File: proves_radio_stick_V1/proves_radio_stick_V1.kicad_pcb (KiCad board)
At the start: 4 copper layers, 88 x 94.5 mm, 54 parts, among them IC2 AZ1117CH-3.3TRG1, J12 USB_C_Receptacle_USB2.0_16P, J22 SWD Port, SW1 KMR2, SW2 KMR2, SW3 SW_Push_SPDT, U11 W25Q128JVS, U18 RP2350_60QFN, Y1 ABM8-272-T3

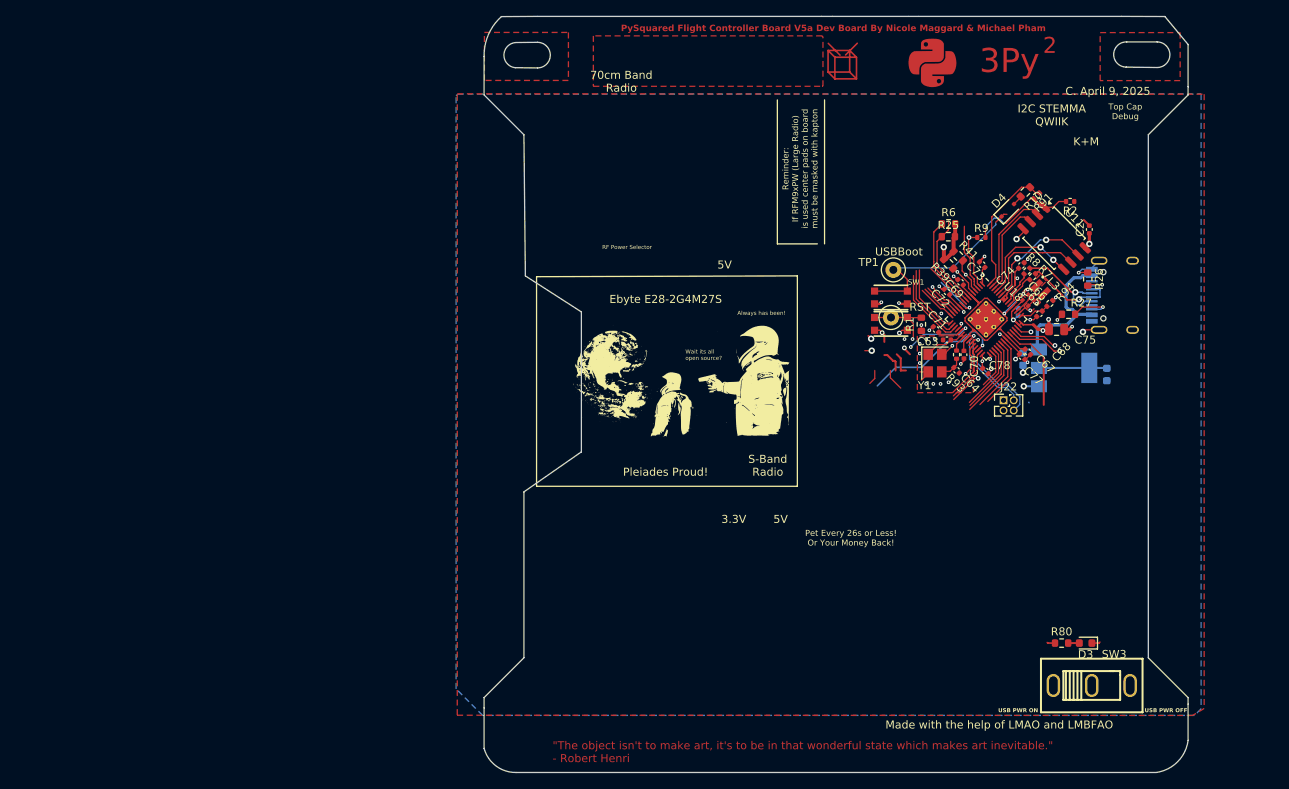
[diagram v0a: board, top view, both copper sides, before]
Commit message: Removed V0a Project
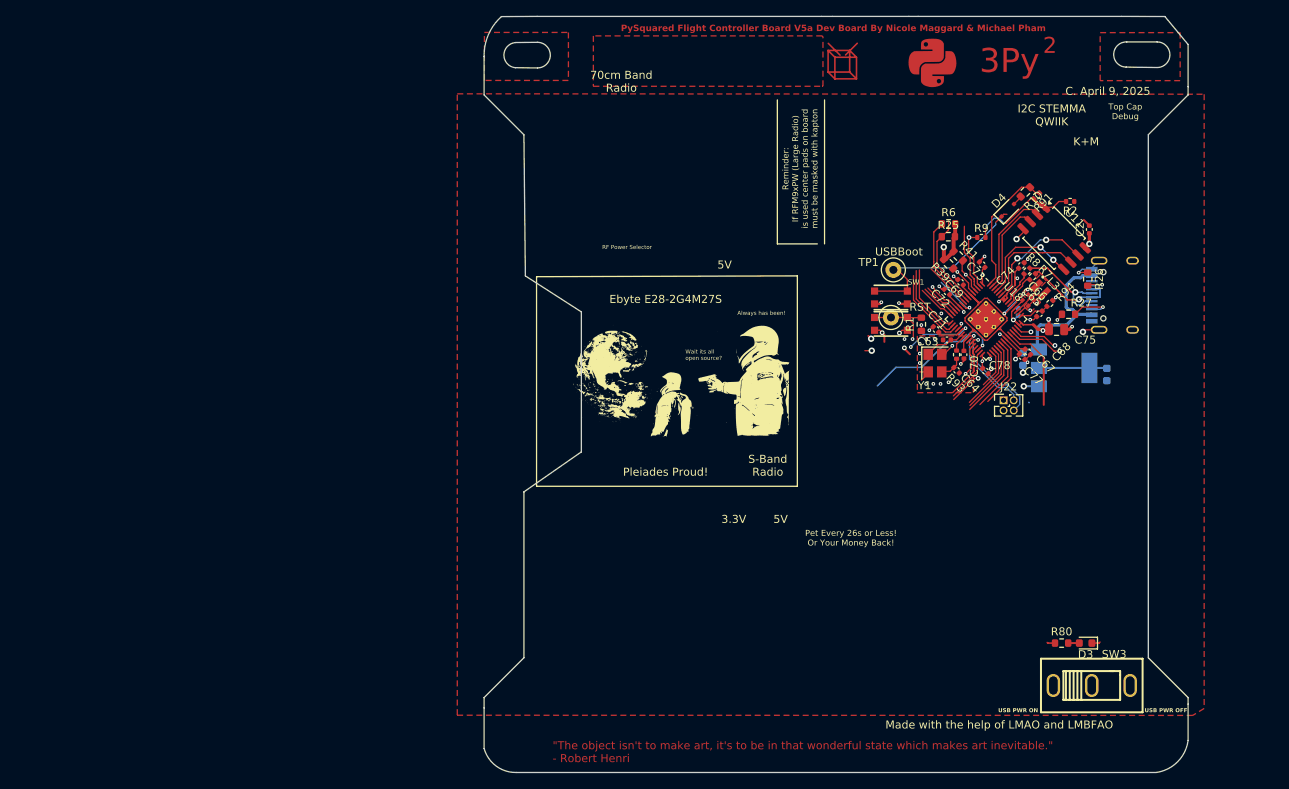
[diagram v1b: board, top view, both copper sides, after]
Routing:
- net (no net): track 9.08 -> 1.48 mm
- net ~{GPIO_EXPANDER_RESET}: track 7.63 -> 4.90 mm
- removed copper zone on B.Cu, net GND
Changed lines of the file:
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@@
 	)
 	(segment
-		(start 195.425 90.3)
-		(end 194.925 89.8)
-		(width 0.25)
-		(layer "F.Cu")
-		(net 0)
-	)
-	(segment
-		(start 192.175 91.825)
-		(end 192.175 92.8294)
-		(width 0.1524)
-		(layer "F.Cu")
-		(net 0)
-	)
-	(segment
-		(start 194.775 91.825)
-		(end 194.775 90.723001)
-		(width 0.25)
-		(layer "F.Cu")
-		(net 0)
-	)
-	(segment
-		(start 195.425 91.825)
-		(end 195.425 90.3)
-		(width 0.25)
-		(layer "F.Cu")
-		(net 0)
-	)
-	(segment
-		(start 192.175 92.8294)
-		(end 191.562475 93.441925)
-		(width 0.1524)
-		(layer "F.Cu")
-		(net 0)
-	)
-	(segment
-		(start 193.75 89.9)
-		(end 193.375 89.9)
-		(width 0.25)
-		(layer "F.Cu")
-		(net 0)
-	)
-	(segment
-		(start 194.676 90.624001)
-		(end 194.474001 90.624001)
-		(width 0.25)
-		(layer "F.Cu")
-		(net 0)
-	)
-	(segment
-		(start 194.474001 90.624001)
-		(end 193.75 89.9)
-		(width 0.25)
-		(layer "F.Cu")
-		(net 0)
-	)
-	(segment
 		(start 191.72272 87.850001)
 		(end 191.374 87.501281)
@@
 		(net 0)
 	)
-	(segment
-		(start 195.425 91.825)
-		(end 196.075 91.825)
-		(width 0.25)
-		(layer "F.Cu")
-		(net 0)
-	)
-	(segment
-		(start 194.775 90.723001)
-		(end 194.676 90.624001)
-		(width 0.25)
-		(layer "F.Cu")
-		(net 0)
-	)
 	(via
 		(at 191.72272 87.850001)
@@
 	)
 	(segment
-		(start 194.125 92.725)
-		(end 195.4238 94.0238)
-		(width 0.1524)
-		(layer "F.Cu")
-		(net 56)
-	)
-	(segment
-		(start 194.125 91.825001)
-		(end 194.125 92.725)
-		(width 0.1524)
-		(layer "F.Cu")
-		(net 56)
-	)
-	(segment
 		(start 207.3 92.048862)
 		(end 207.3 90.032753)
@@
 			)
 		)
-	)
-	(zone
-		(net 1)
-		(net_name "GND")
-		(layer "B.Cu")
-		(hatch edge 0.5)
-		(priority 4)
-		(connect_pads
-			(clearance 0.5)
-		)
-		(min_thickness 0.25)
-		(filled_areas_thickness no)
-		(fill yes
-			(thermal_gap 0.5)
-			(thermal_bridge_width 0.5)
-		)
-		(polygon
-			(pts
-				(xy 140.07 57.27) (xy 232.97 57.27) (xy 232.97 134.11) (xy 232.14 134.94) (xy 143.16 134.94) (xy 139.84 131.62)
-				(xy 139.84 57.5)
-			)
-		)

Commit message: Initial TPS62 Layout
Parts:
- added C14: 22uF, Capacitor_SMD:C_0603_1608Metric, F.Cu at (212.3, 107.8)
- added C15: 10uF, Capacitor_SMD:C_0603_1608Metric, F.Cu at (210.0, 107.0)
- added L1: XFL4015-471MEC, easyeda2kicad:IND-SMD_L4.0-W4.0_XFL4020-102MEB, F.Cu at (211.1, 104.0)
- added R3: 162k, Resistor_SMD:R_0603_1608Metric, F.Cu at (212.3, 110.8)
- added R4: 510k, Resistor_SMD:R_0603_1608Metric, F.Cu at (210.0, 111.6)
- added U1: E22-400M30S, easyeda2kicad:WIRELM-SMD_E22-400M30S, F.Cu at (98.2, 74.6)
- added U2: TPS62085RLTT, easyeda2kicad:VSON-7_L2.0-W2.0-P0.5-TL, F.Cu at (210.0, 109.3)
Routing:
- net SPI1_CS1: track 14.4 -> 1.05 mm
- net RF2_IO0: track 10.0 -> 4.00 mm
- net RF2_TX_EN: track 9.08 -> 3.57 mm
- net RF2_RX_EN: track 8.29 -> 3.13 mm
- net WDT_WDI: track 9.46 -> 4.54 mm
- net Net-(U2-SW): track 0.00 -> 4.50 mm
- net SPI1_SCK: track 6.80 -> 2.56 mm
- net SPI1_MOSI: track 7.78 -> 3.62 mm
- net WDT_ENABLE: track 9.17 -> 5.07 mm
- net +3V3: track 81.2 -> 85.2 mm, vias 18 -> 19
- net SPI1_MISO: track 6.96 -> 3.14 mm
- net Net-(U2-FB): track 0.00 -> 3.35 mm
- net GND: track 50.2 -> 47.4 mm, vias 34 -> 40
- net ~{GPIO_EXPANDER_RESET}: track 4.90 -> 2.70 mm
- net (no net): track 1.48 -> 0.07 mm, vias 1 -> 0

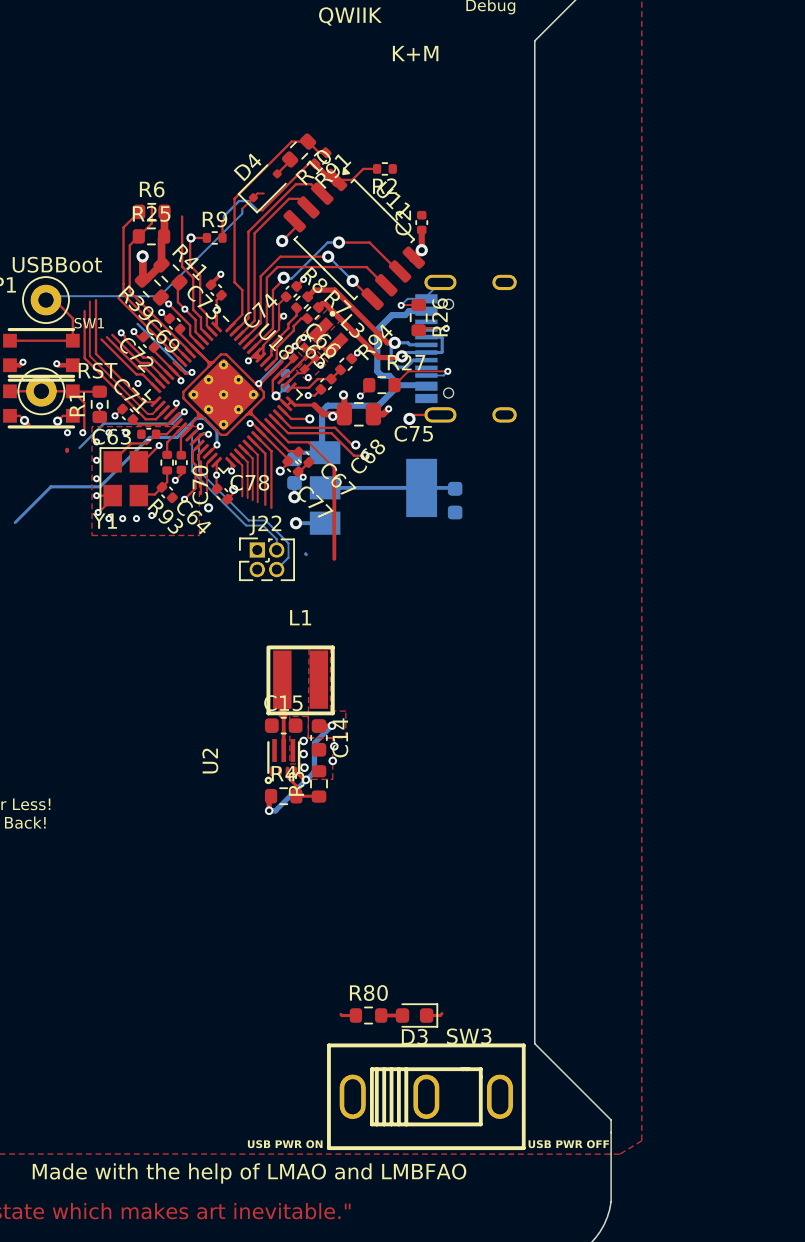
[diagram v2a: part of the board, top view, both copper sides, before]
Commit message: Removed 3v3 Linear Regulator
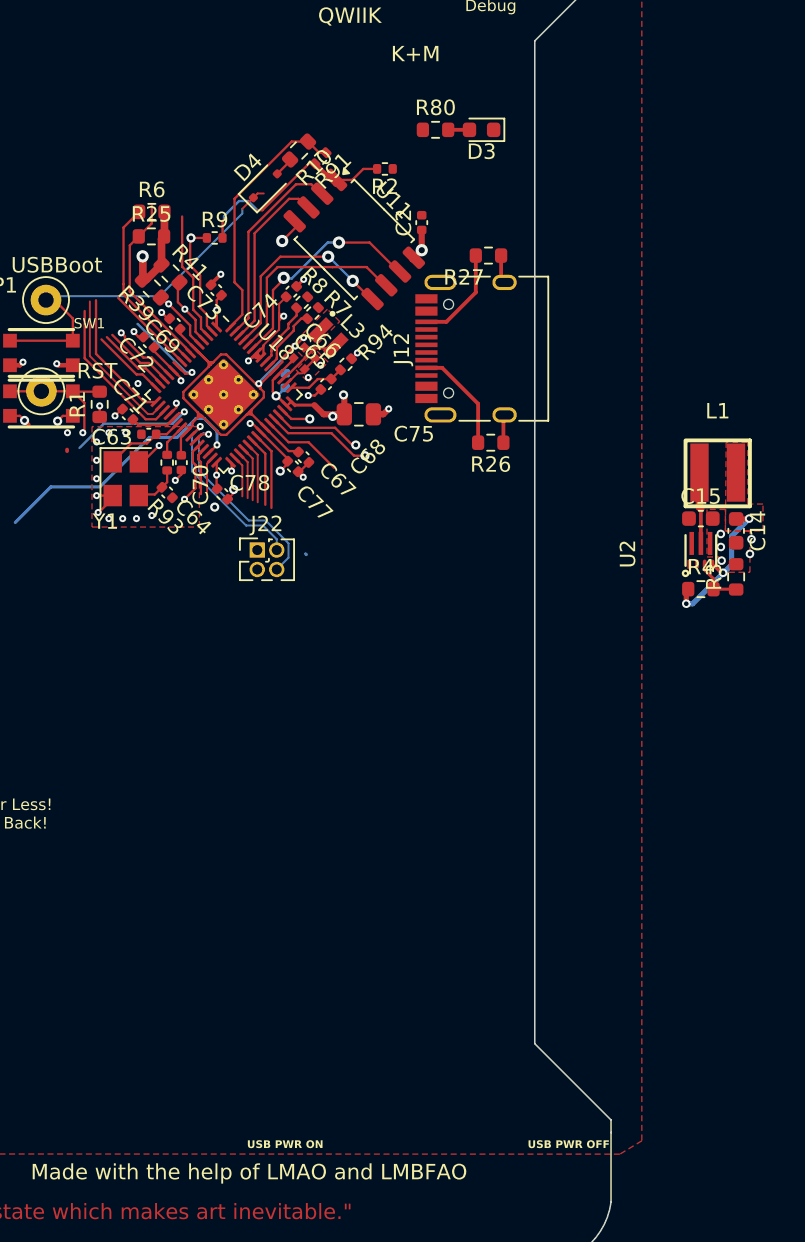
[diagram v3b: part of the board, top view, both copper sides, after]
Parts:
- removed C12: 10uF, Capacitor_SMD:C_0603_1608Metric
- removed C13: 22uF, Capacitor_SMD:C_0603_1608Metric
- removed IC2: AZ1117CH-3.3TRG1, Package_TO_SOT_SMD:SOT-223
- removed SW3: SW_Push_SPDT, easyeda2kicad:SW-TH_SHOU-HAN_SS12D10G4
- J12: moved to F.Cu
- R80: value 100k -> 10k
- moved D3 57.9 mm to (222.9, 68.2)
- moved R80 57.9 mm to (219.9, 68.2)
- moved L1 30.4 mm to (238.3, 90.5)
- moved C14 30.4 mm to (239.5, 94.3)
- moved C15 30.4 mm to (237.2, 93.5)
- moved R3 30.4 mm to (239.5, 97.3)
- moved R4 30.4 mm to (237.2, 98.1)
- moved U2 30.4 mm to (237.2, 95.8)
- moved R27 10.9 mm to (223.3, 76.3), turned to 180 degrees
- moved R26 9.41 mm to (223.5, 88.5), turned to 180 degrees
- turned J12 to 90 degrees
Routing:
- net VBUS: track 21.1 -> 0.00 mm
- net USB_D+: track 13.9 -> 0.00 mm, vias 1 -> 0
- net USB_D-: track 11.7 -> 0.00 mm, vias 1 -> 0
- net /3v3 Spec: track 8.39 -> 0.00 mm
- net GND: track 47.4 -> 39.7 mm, vias 40 -> 35
- net ~{MUX_RESET}: track 11.4 -> 5.43 mm
- net Net-(J12-CC1): track 3.18 -> 6.88 mm, vias 1 -> 0
- net Net-(J12-CC2): track 5.35 -> 6.42 mm, vias 1 -> 0
- net +3V3: track 85.2 -> 84.1 mm

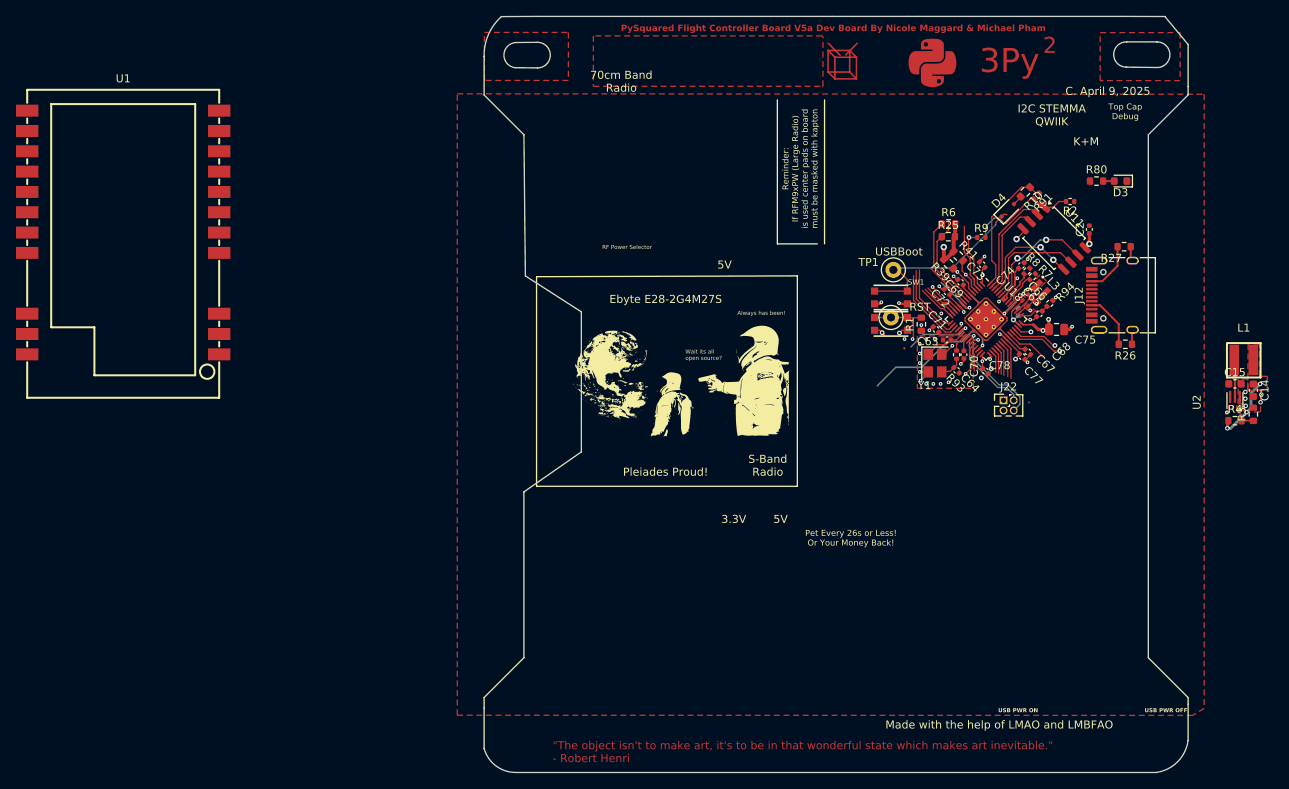
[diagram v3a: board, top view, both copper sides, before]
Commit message: RP2350 and Support Circuits Layout
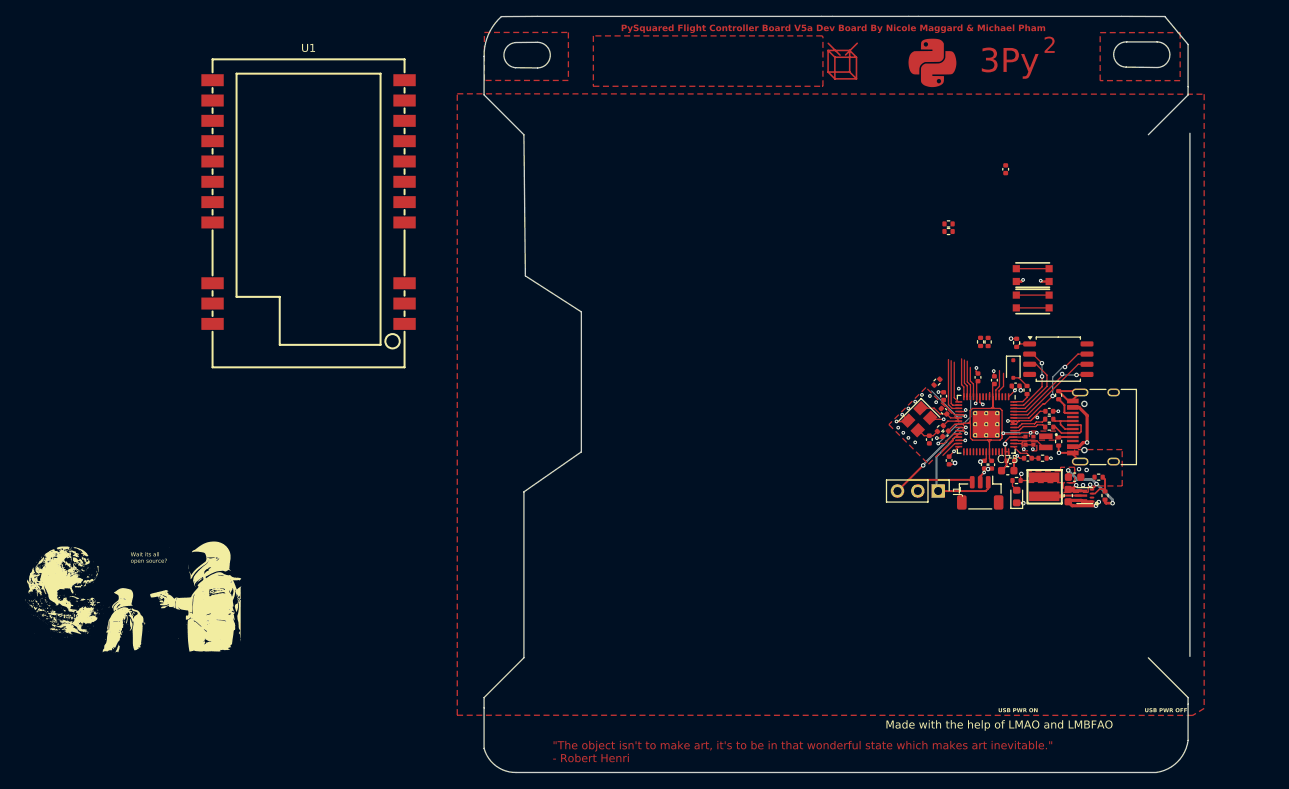
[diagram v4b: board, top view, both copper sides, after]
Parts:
- removed the G*** at (186.3, 67.3)
- removed R9: DNF, Resistor_SMD:R_0402_1005Metric
- removed R91: 0, Resistor_SMD:R_0402_1005Metric
- removed TP1: USBBOOT, TestPoint:TestPoint_Loop_D1.80mm_Drill1.0mm_Beaded
- removed TP2: RESET, TestPoint:TestPoint_Loop_D1.80mm_Drill1.0mm_Beaded
- added J1: SWD Port, Connector_PinHeader_2.54mm:PinHeader_1x03_P2.54mm_Vertical, F.Cu at (200.1, 106.9)
- C75: footprint Capacitor_SMD:C_0805_2012Metric -> Capacitor_SMD:C_0603_1608Metric
- C76: moved to F.Cu
- J22: footprint Connector_PinHeader_1.27mm:PinHeader_2x02_P1.27mm_Vertical -> Connector_JST:JST_SH_BM03B-SRSS-TB_1x03-1MP_P1.00mm_Vertical
- R1, R10, R25, R26, R27, R3, R39, R4, R41, R6, R80: footprint Resistor_SMD:R_0603_1608Metric -> Resistor_SMD:R_0402_1005Metric
- moved G*** 73.6 mm to (98.6, 119.7)
- moved D3 41.5 mm to (209.9, 107.6), turned to 90 degrees
- moved R80 38.7 mm to (209.9, 105.6), turned to 180 degrees
- moved L1 29.6 mm to (213.4, 106.4), turned to 90 degrees
- moved C15 25.1 mm to (216.4, 107.5), turned to 90 degrees
- moved C14 24.8 mm to (217.2, 105.2), turned to 0 degrees
- moved R10 24.8 mm to (211.2, 94.3), turned to 90 degrees
- moved U1 23.5 mm to (121.4, 70.8)
- moved U2 21.9 mm to (218.7, 107.5), turned to 180 degrees
- moved R3 20.9 mm to (220.2, 105.2), turned to 180 degrees
- moved R27 20.3 mm to (215.2, 94.9), turned to -90 degrees
- moved D4 19.9 mm to (209.5, 91.6), turned to -90 degrees
- moved R94 19.4 mm to (213.2, 102.8), turned to 180 degrees
- moved L3 19.1 mm to (213.6, 100.7), turned to -90 degrees
- moved R7 18.9 mm to (214.0, 98.9), turned to 0 degrees
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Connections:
- J22 pad 1: FC_RESET -> SWDIO
- J22 pad 2: SWCLK -> GND
- J22 pad 3: GND -> SWCLK
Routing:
- net +3V3: track 84.1 -> 54.4 mm, vias 19 -> 14
- net VBUS: track 0.00 -> 24.0 mm, vias 0 -> 3
- net /USBBOOT: track 24.5 -> 4.10 mm
- net RF2_RST: track 18.0 -> 0.82 mm
- net BOOTSEL: track 16.3 -> 2.30 mm
- net FC_RESET: track 28.7 -> 15.2 mm, vias 2 -> 1
- net GND: track 39.7 -> 53.0 mm, vias 35 -> 33
- net /FLASH_SS: track 14.4 -> 1.78 mm
- net SCL0: track 11.6 -> 0.00 mm
- net SDA0: track 11.8 -> 0.54 mm
- net SWCLK: track 12.1 -> 20.9 mm, vias 1 -> 2
- net RX: track 8.47 -> 0.00 mm
- net TX: track 7.76 -> 0.00 mm, vias 1 -> 0
- net RTC_INT: track 7.08 -> 0.00 mm, vias 1 -> 0
- net RF1_RST: track 5.89 -> 0.00 mm
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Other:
- board size 88 x 94.5 mm -> 88.2 x 94.5 mm
- board text removed: "0x18 0x77 0x6B 0x1E"
- board text removed: "3.3V"
- board text removed: "3v3"
- board text removed: "3v3 Reg"
- board text removed: "5V"
- board text removed: "70cm Band Radio"
- board text removed: "Address"
- board text removed: "Always has been!"
- board text removed: "C. April 9, 2025"
- board text removed: "Ebyte E28-2G4M27S"
- board text removed: "GND"
- board text removed: "Hubble Space Telescope Nebulosity in The Pleiades"
- board text removed: "I2C Devices"
- board text removed: "I2C STEMMA QWIIK"
- board text removed: "K+M"
- board text removed: "MCP9808 TCA9548A LSM6DSO LSM303AGR RV3028 INA219-Sys INA219-Sol MCP23017SS"
- board text removed: "Pet Every 26s or Less! Or Your Money Back!"
- board text removed: "Pleiades Proud!"
- board text removed: "RF Power Selector"
- board text removed: "RST"
- board text removed: "RX"
- board text removed: "Reminder: If RFM9xPW (Large Radio) is used center pads on board must be masked with kapton"
- board text removed: "S-Band Radio"
- board text removed: "SCL1"
- board text removed: "SDA1"
- board text removed: "TX"
- board text removed: "Top Cap Debug"
- board text removed: "USBBoot"

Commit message: Added E32 Footprint
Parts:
- removed U1: E22-400M30S, easyeda2kicad:WIRELM-SMD_E22-400M30S
- added U3: E32-400M20S_C2965514, easyeda2kicad:WIRELM-SMD_E32-400M20S, F.Cu at (171.1, 97.4)
